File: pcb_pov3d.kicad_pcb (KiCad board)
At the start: 4 copper layers, 92 parts, among them P1 CONN_4X2, P2 CONN_6, P3 MICRO-SD, P4 CONN_2, P5 KNUSB, P6 CONN_12, U1 TLC5955, U2 TLC5955, U3 TLC5955, U4 STM32F40X_LQFP64, U5 US4881_HALL, U6 LP38691, X1 CRYSTAL

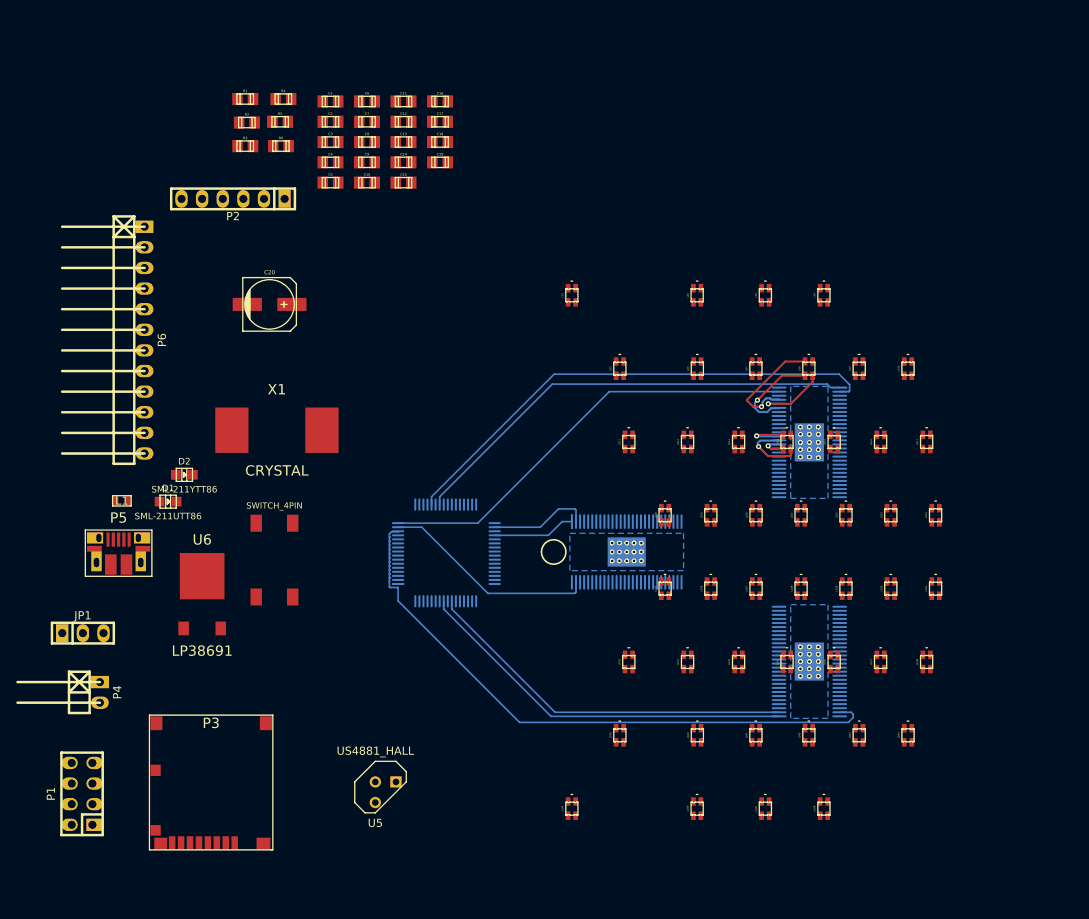
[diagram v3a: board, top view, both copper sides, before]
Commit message: LED routing, and initial placement of most remaining components.
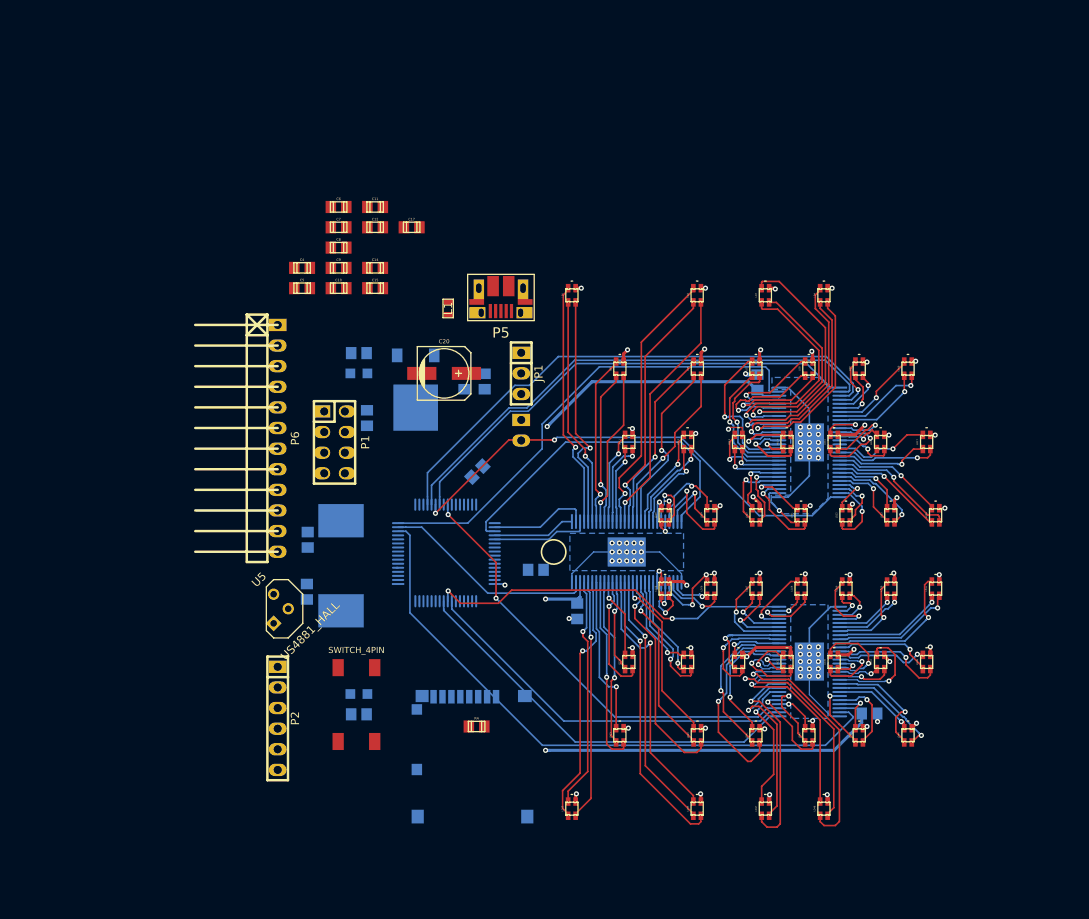
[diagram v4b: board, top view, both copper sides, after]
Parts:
- C1, C13, C16, C18, C19, C2, C3, D1, D2, P3, P4, R1, R2, R3, R5, R6, U6, X1: moved to B.Cu
- moved C3 96.8 mm to (138.9, 119.9), turned to 180 degrees
- moved R4 80.9 mm to (90.5, 121.5)
- moved R6 70.7 mm to (76.0, 120.0)
- moved C2 67.5 mm to (102.9, 107.3), turned to 90 degrees
- moved P2 64.2 mm to (66.0, 120.5), turned to 270 degrees
- moved C1 63.0 mm to (125.1, 79.1), turned to 270 degrees
- moved JP1 62.8 mm to (96.0, 78.0), turned to 270 degrees
- moved P4 61.1 mm to (96.0, 85.0)
- moved C16 58.9 mm to (97.8, 102.2), turned to 180 degrees
- moved P5 58.0 mm to (93.5, 67.5), turned to 180 degrees
- moved C18 57.8 mm to (69.6, 104.9), turned to 270 degrees
- moved P1 53.3 mm to (73.0, 86.5), turned to 270 degrees
- moved C19 49.3 mm to (69.7, 98.5), turned to 90 degrees
- moved L1 46.7 mm to (87.0, 70.0), turned to 90 degrees
- moved R1 45.6 mm to (91.5, 79.0), turned to 90 degrees
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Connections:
- net Net-(C13-Pad1) renamed /MCU_Pwr/vcap1
- net Net-(C16-Pad1) renamed /MCU_Pwr/vcap2
- U3 pad 42: /LEDs/led37g -> /LEDs/led36g
- U3 pad 43: /LEDs/led37r -> /LEDs/led36r
- U3 pad 44: /LEDs/led37b -> /LEDs/led36b
- U3 pad 45: /LEDs/led36g -> /LEDs/led37g
- U3 pad 46: /LEDs/led36r -> /LEDs/led37r
- U3 pad 47: /LEDs/led36b -> /LEDs/led37b
- U4 pad 20: Net-(U4-Pad20) -> /LEDs/lat1
- U4 pad 24: /LEDs/lat1 -> Net-(U4-Pad24)
- U4 pad 25: /LEDs/lat2 -> /LEDs/lat3
- U4 pad 37: /LEDs/lat3 -> /LEDs/lat2
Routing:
- net +5V: track 0.00 -> 405.4 mm, vias 0 -> 46
- net GND: track 0.74 -> 150.2 mm, vias 45 -> 48
- net +3.3V: track 0.00 -> 130.2 mm, vias 0 -> 4
- net /LEDs/lat1: track 0.00 -> 66.5 mm
- net /LEDs/sout1: track 0.00 -> 59.7 mm, vias 0 -> 2
- net /LEDs/lat3: track 0.00 -> 55.4 mm, vias 0 -> 2
- net /LEDs/sout3: track 0.00 -> 45.4 mm, vias 0 -> 2
- net /LEDs/sout2: track 0.00 -> 42.0 mm
- net /LEDs/led46r: track 0.00 -> 35.2 mm, vias 0 -> 1
- net /LEDs/led2b: track 0.00 -> 33.2 mm, vias 0 -> 1
- net /LEDs/led46b: track 0.00 -> 32.3 mm, vias 0 -> 1
- net /LEDs/led46g: track 0.00 -> 32.1 mm, vias 0 -> 1
- net /LEDs/led48g: track 0.00 -> 31.5 mm, vias 0 -> 1
- net /LEDs/led45g: track 0.00 -> 31.2 mm, vias 0 -> 1
- net /LEDs/led2r: track 0.00 -> 30.9 mm, vias 0 -> 1
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- added copper zone on In1.Cu, net +5V

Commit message: Routing
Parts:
- C13: moved to F.Cu
- C14, C15, C20, C4, JP1: moved to B.Cu
- moved C17 66.1 mm to (77.0, 125.9)
- moved C5 58.0 mm to (89.6, 121.7), turned to 90 degrees
- moved C4 45.2 mm to (68.1, 110.2), turned to 225 degrees
- moved C20 17.1 mm to (103.0, 73.7), turned to 180 degrees
- moved R1 16.0 mm to (95.1, 63.4)
- moved R2 15.8 mm to (92.7, 63.6)
- moved C14 15.3 mm to (91.4, 72.3), turned to 90 degrees
- moved P1 12.5 mm to (74.6, 74.1), turned to 180 degrees
- moved C15 10.1 mm to (83.7, 75.8)
- moved L1 8.88 mm to (78.3, 68.2)
- moved P5 8.41 mm to (85.1, 67.2)
- moved D1 8.00 mm to (76.1, 86.0)
- moved R5 7.70 mm to (76.0, 83.2)
- moved U6 6.20 mm to (89.2, 79.1)
- moved R3 5.32 mm to (77.4, 78.2), turned to 180 degrees
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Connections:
- P5 pad 4: /MCU_Pwr/usb_dm -> /MCU_Pwr/usb_id
- U4 pad 43: /MCU_Pwr/usb_dm -> /MCU_Pwr/usb_id
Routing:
- net GND: track 150.2 -> 237.1 mm, vias 48 -> 61
- net /MCU_Pwr/vusb: track 0.00 -> 49.4 mm, vias 0 -> 1
- net /nrf_ck: track 0.00 -> 47.9 mm, vias 0 -> 1
- net /nrf_miso: track 0.00 -> 40.2 mm, vias 0 -> 1
- net /MCU_Pwr/usb_dp: track 0.00 -> 40.0 mm, vias 0 -> 1
- net /MCU_Pwr/usb_dm: track 0.00 -> 39.4 mm, vias 0 -> 1
- net /MCU_Pwr/usb_id: track 0.00 -> 38.0 mm, vias 0 -> 1
- net /nrf_mosi: track 0.00 -> 36.2 mm, vias 0 -> 1
- net /nrf_cs: track 0.00 -> 33.5 mm, vias 0 -> 1
- net /nrf_ce: track 0.00 -> 30.9 mm
- net /nrf_irq: track 0.00 -> 29.2 mm, vias 0 -> 1
- net /sd_cd: track 0.00 -> 26.5 mm, vias 0 -> 2
- net /sd_d0: track 0.00 -> 24.2 mm, vias 0 -> 2
- net /sd_d1: track 0.00 -> 22.1 mm, vias 0 -> 2
- net +5V: track 405.4 -> 426.4 mm, vias 46 -> 50
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
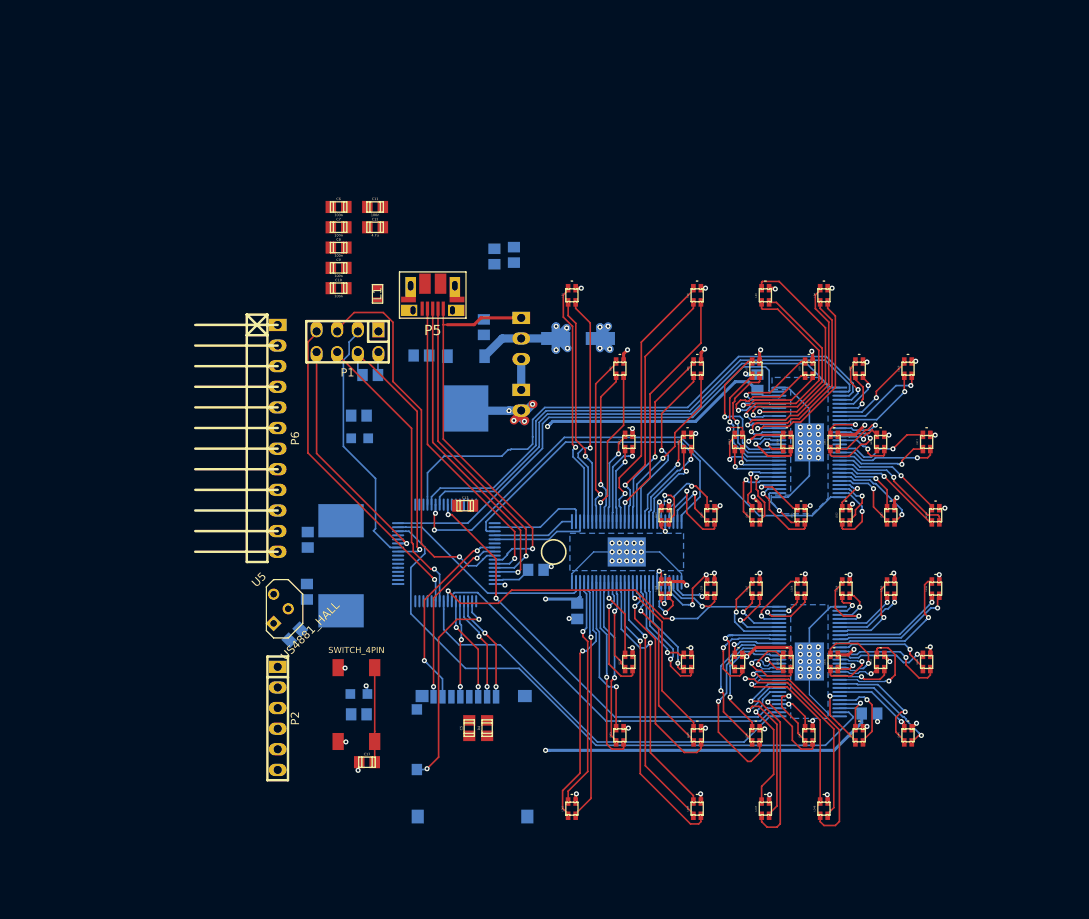
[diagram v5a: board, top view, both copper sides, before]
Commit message: Most signals routed (still some power/gnd to route)
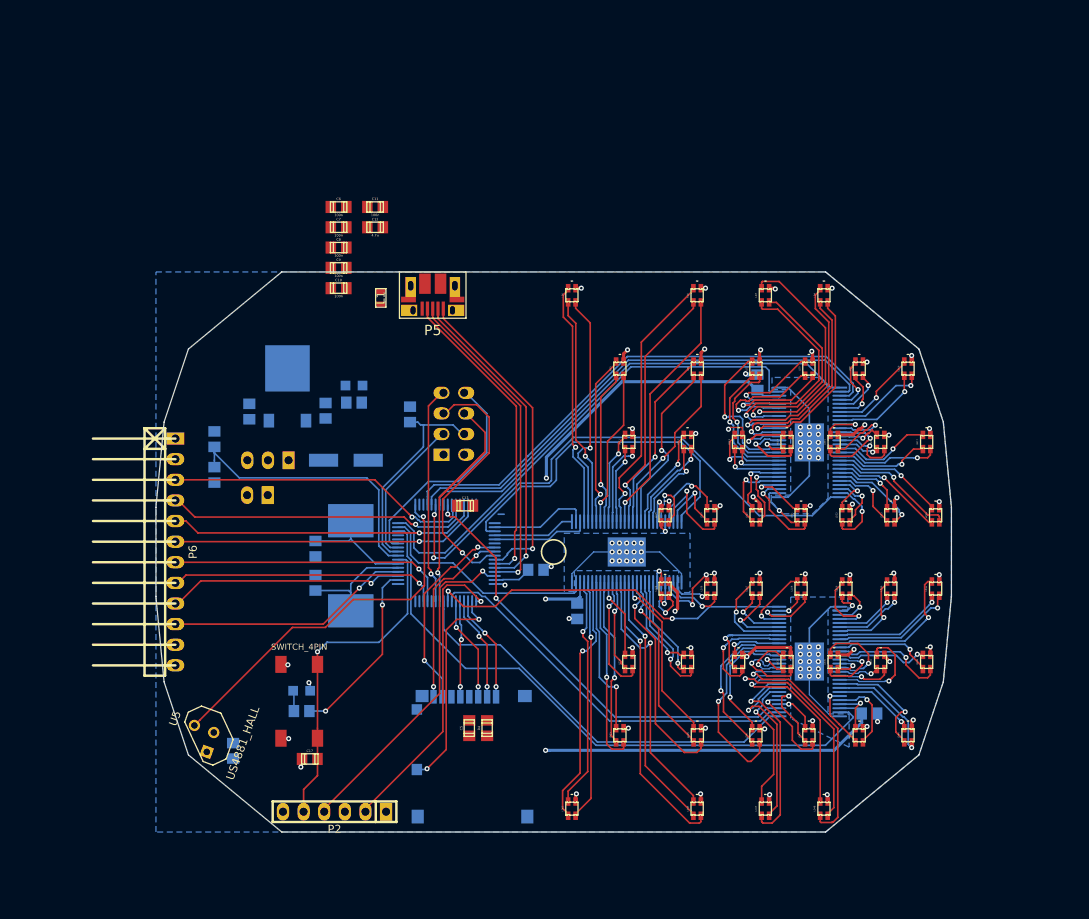
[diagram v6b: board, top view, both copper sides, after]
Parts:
- P1: moved to B.Cu
- moved R2 43.7 mm to (58.2, 90.5), turned to 90 degrees
- moved R1 43.3 mm to (58.2, 86.1)
- moved JP1 34.6 mm to (64.8, 88.7), turned to 180 degrees
- moved P4 34.5 mm to (63.5, 93.0), turned to 180 degrees
- moved C20 32.3 mm to (74.4, 88.7)
- moved C14 30.7 mm to (62.5, 82.7), turned to 270 degrees
- moved U6 22.1 mm to (67.2, 80.6), turned to 180 degrees
- moved P6 18.8 mm to (53.4, 100.0)
- moved U5 18.4 mm to (56.5, 123.0), turned to 250 degrees
- moved P1 16.5 mm to (87.7, 84.2), turned to 90 degrees
- moved C4 16.2 mm to (60.5, 124.5), turned to 270 degrees
- moved C15 13.6 mm to (71.9, 82.6), turned to 270 degrees
- moved P2 13.5 mm to (73.0, 132.0), turned to 180 degrees
- moved C17 7.06 mm to (70.0, 125.5)
- moved D2 7.06 mm to (69.0, 117.1)
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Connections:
- P6 pad 10: /usart3_rx -> /pc15
- P6 pad 5: /pb2 -> /usart3_tx
- P6 pad 6: /pb8 -> /usart3_rx
- P6 pad 7: /pb9 -> /pb8
- P6 pad 8: /pb12 -> /pb9
- P6 pad 9: /usart3_tx -> /pc14
- U4 pad 2: Net-(U4-Pad2) -> /MCU_Pwr/user_led
- U4 pad 28: /pb2 -> Net-(U4-Pad28)
- U4 pad 3: Net-(U4-Pad3) -> /pc14
- U4 pad 33: /pb12 -> Net-(U4-Pad33)
- U4 pad 38: /MCU_Pwr/user_led -> Net-(U4-Pad38)
- U4 pad 4: Net-(U4-Pad4) -> /pc15
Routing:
- net GND: track 237.1 -> 183.1 mm, vias 61 -> 53
- net /hall: track 0.00 -> 46.2 mm, vias 0 -> 1
- net /swdio: track 0.00 -> 41.4 mm, vias 0 -> 1
- net /usart3_rx: track 0.00 -> 38.8 mm, vias 0 -> 1
- net /usart3_tx: track 0.00 -> 38.4 mm, vias 0 -> 1
- net /pb0: track 0.00 -> 38.2 mm, vias 0 -> 1
- net /pb1: track 0.00 -> 38.1 mm, vias 0 -> 1
- net /swclk: track 0.00 -> 37.7 mm, vias 0 -> 1
- net /bat_sense: track 0.00 -> 35.3 mm
- net /pb8: track 0.00 -> 34.8 mm, vias 0 -> 1
- net /pb9: track 0.00 -> 33.3 mm, vias 0 -> 1
- net /pc15: track 0.00 -> 30.1 mm, vias 0 -> 1
- net /MCU_Pwr/nrst: track 11.6 -> 41.2 mm, vias 0 -> 1
- net /pc14: track 0.00 -> 29.1 mm, vias 0 -> 1
- net /MCU_Pwr/user_led: track 0.00 -> 22.4 mm, vias 0 -> 2
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- added copper zone on In2.Cu, net GND
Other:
- board outline added: 98 x 69 mm

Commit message: Complete routing
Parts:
- added C21: 100n, w_smd_cap:c_0805, B.Cu at (58.1, 93.3)
- C10, C11, C12, C13, C6, C7, C9: moved to B.Cu
- moved C6 52.3 mm to (84.4, 108.7)
- moved C12 51.3 mm to (84.4, 110.9)
- moved C7 49.7 mm to (96.1, 104.3)
- moved C11 48.7 mm to (80.5, 106.1), turned to 270 degrees
- moved C8 36.6 mm to (80.9, 98.3), turned to 225 degrees
- moved C10 31.4 mm to (92.3, 92.7), turned to 45 degrees
- moved C9 28.4 mm to (82.4, 92.0), turned to 225 degrees
- moved C13 2.14 mm to (88.7, 92.2)
- moved C16 0.82 mm to (97.0, 102.4)
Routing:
- net GND: track 183.1 -> 457.2 mm, vias 53 -> 74
- net +3.3V: track 128.3 -> 336.2 mm, vias 4 -> 16
- net +5V: track 409.9 -> 513.1 mm, vias 46 -> 50
- net /MCU_Pwr/vusb: track 39.5 -> 83.1 mm, vias 1 -> 2
- net Net-(L1-Pad2): track 0.00 -> 18.3 mm
- net /nrf_mosi: track 34.6 -> 27.3 mm
- net /bat_sense: track 35.3 -> 41.0 mm
- net /MCU_Pwr/bat_vcc: track 0.00 -> 5.34 mm
- net /LEDs/sout1: track 69.3 -> 64.5 mm
- net (no net): track 0.74 -> 4.20 mm
- net /LEDs/gsclk1: track 61.9 -> 58.8 mm
- net /sd_d3: track 13.0 -> 15.9 mm, vias 2 -> 3
- net /LEDs/led41r: track 24.4 -> 21.8 mm
- net /nrf_irq: track 27.8 -> 30.4 mm
- net Net-(D1-Pad1): track 0.00 -> 2.14 mm
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- added copper zone on In1.Cu, net +3.3V
- added copper zone on F.Cu, net GND

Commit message: Routing tweaks.
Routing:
- net (no net): track 4.20 -> 0.00 mm
- net /swclk: track 37.6 -> 34.3 mm
- net /swdio: track 41.4 -> 39.3 mm
- net /sd_d0: track 25.2 -> 23.4 mm
- net /sd_cd: track 26.5 -> 25.1 mm
- net /LEDs/sout3: track 45.8 -> 45.1 mm
- net /sd_d1: track 22.7 -> 22.1 mm
